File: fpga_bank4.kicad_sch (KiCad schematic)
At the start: 2 parts, among them U2 XC7A50T-FGG484

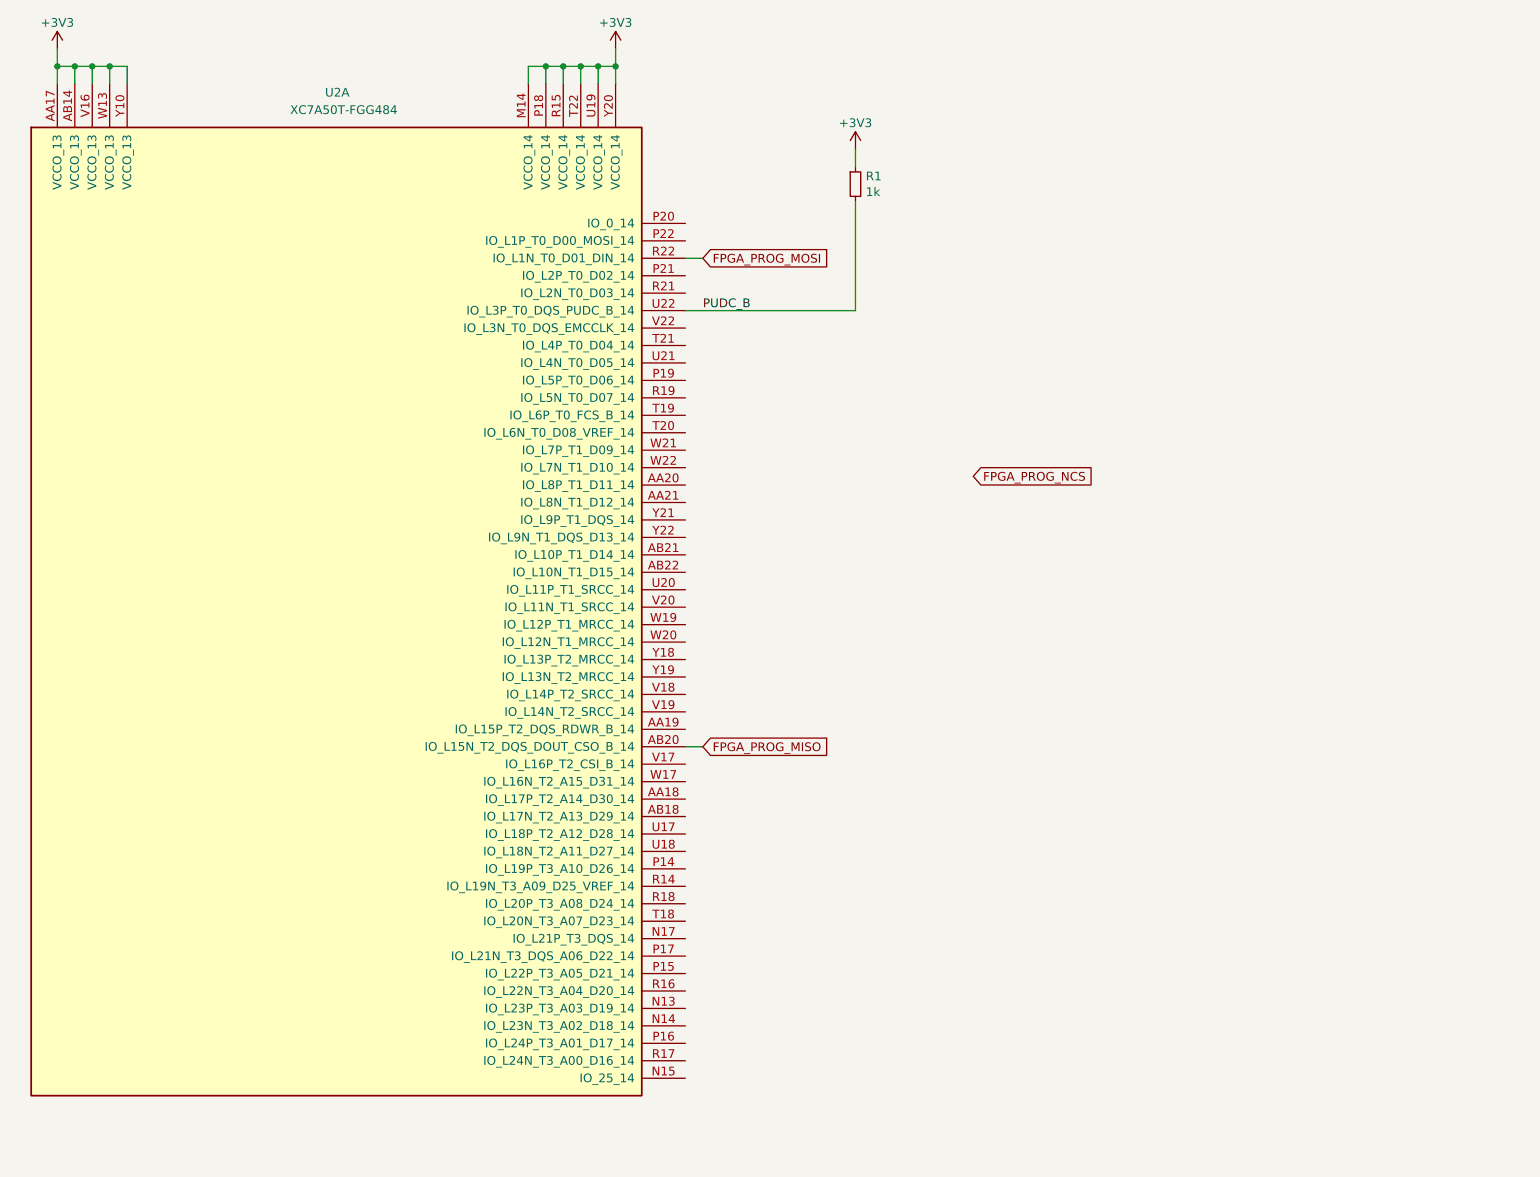
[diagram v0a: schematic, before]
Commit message: Changed FPGA to new package and hooked up some more pins
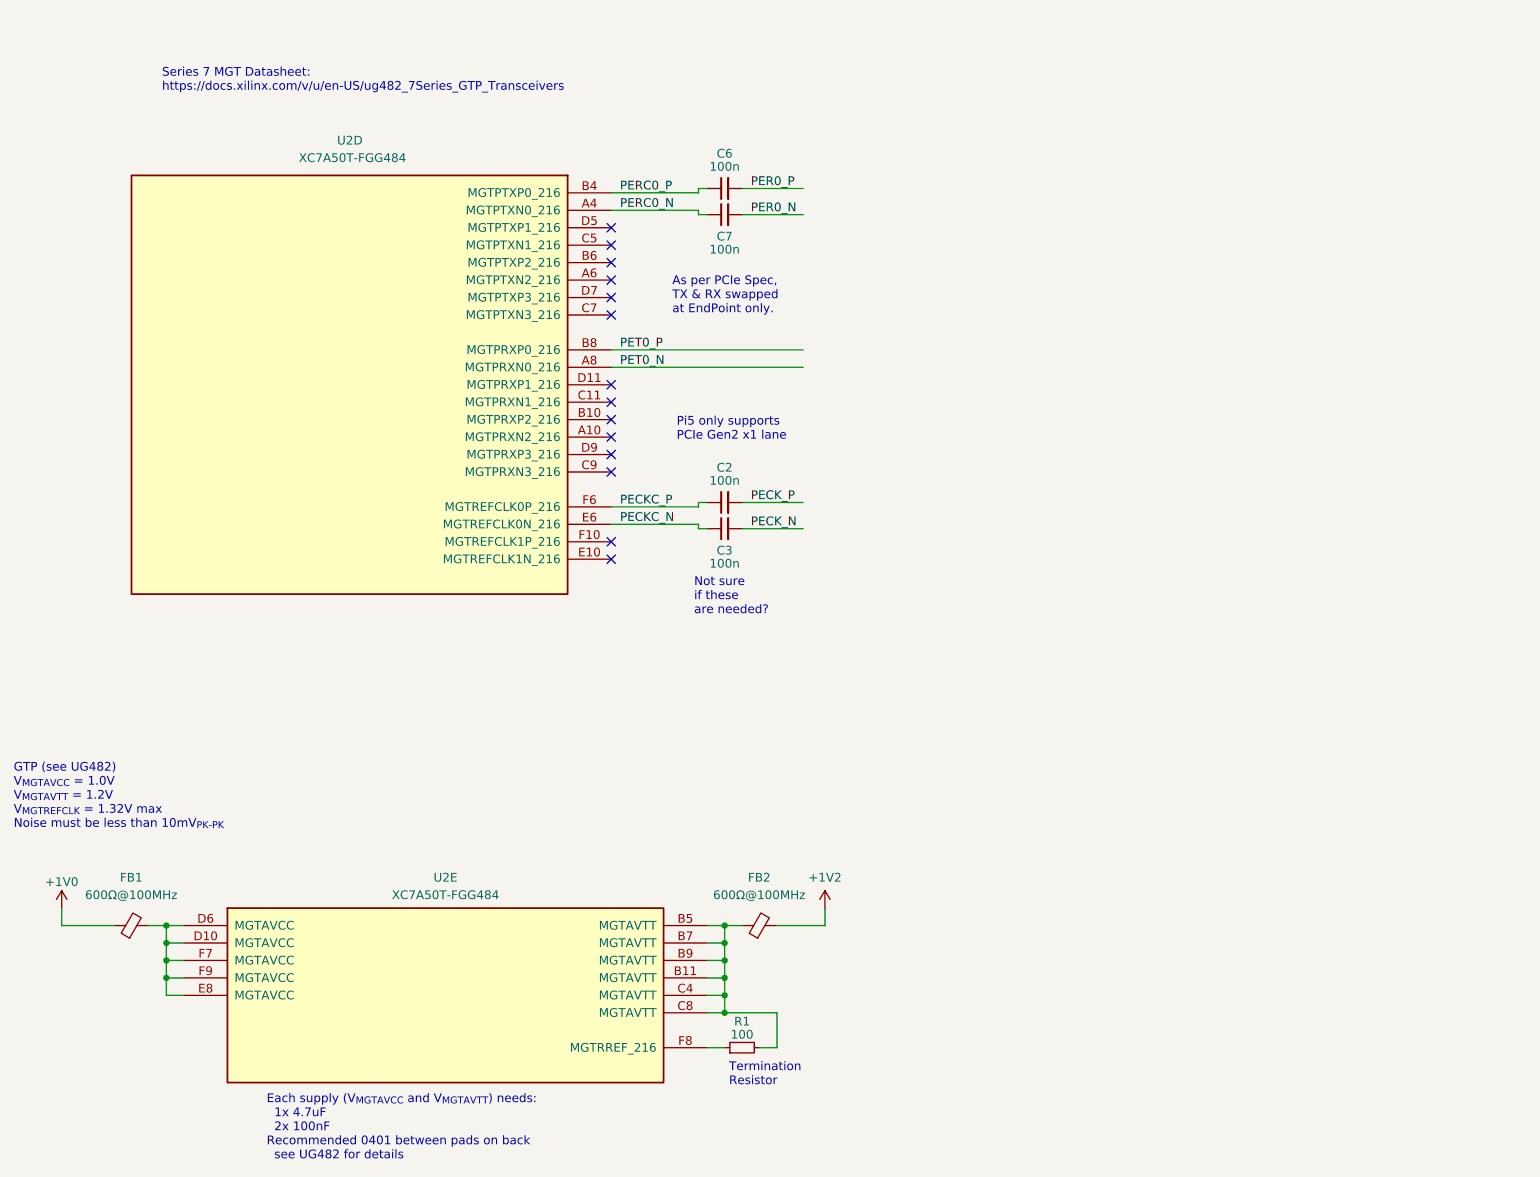
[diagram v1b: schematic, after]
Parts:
- removed U2: XC7A50T-FGG484, Package_BGA:Xilinx_FGG484, symbol FPGA_Xilinx_Artix7:XC7A50T-FGG484
- added C2, C3, C6, C7: 100n, Capacitor_SMD:C_0402_1005Metric_Pad0.74x0.62mm_HandSolder, symbol Device:C_Small
- added FB1, FB2: 600Ω@100MHz, Inductor_SMD:L_0603_1608Metric_Pad1.05x0.95mm_HandSolder, symbol Device:FerriteBead_Small
- added U2: XC7A50T-FGG484, Package_BGA:Xilinx_FGG484, symbol FPGA_Xilinx_Artix7:XC7A50T-FGG484
- R1: value 1k -> 100; LCSC C21190 -> C22775
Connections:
- net +3V3: no longer names the net of R1.1
- net +3V3: now also U2.F8 (MGTRREF_216)
- net PUDC_B: no longer names the net of R1.2
- net PUDC_B: now also FB2.1, U2.B11 (MGTAVTT), U2.B5 (MGTAVTT), U2.B7 (MGTAVTT), U2.B9 (MGTAVTT), U2.C4 (MGTAVTT), U2.C8 (MGTAVTT)
- new net: FB1.2, U2.D10 (MGTAVCC), U2.D6 (MGTAVCC), U2.E8 (MGTAVCC), U2.F7 (MGTAVCC), U2.F9 (MGTAVCC)
- new net +1V0: FB1.1
- new net +1V2: FB2.2
- new net PECKC_N: C3.1, U2.E6 (MGTREFCLK0N_216)
- new net PECKC_P: C2.1, U2.F6 (MGTREFCLK0P_216)
- new net PECK_N: C3.2
- new net PECK_P: C2.2
- new net PER0_N: C7.2
- new net PER0_P: C6.2
- new net PERC0_N: C7.1, U2.A4 (MGTPTXN0_216)
- new net PERC0_P: C6.1, U2.B4 (MGTPTXP0_216)
- new net PET0_N: U2.A8 (MGTPRXN0_216)
- new net PET0_P: U2.B8 (MGTPRXP0_216)
- no-connect marks 0 -> 14
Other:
- note added: "As per PCIe Spec, TX & RX swapped at EndPoint only."
- note added: "Each supply (V_{MGTAVCC} and V_{MGTAVTT}) needs: 1x 4.7uF 2x 100nF Recommended 0401 between pads on back see UG482 for details"
- note added: "GTP (see UG482) V_{MGTAVCC} = 1.0V V_{MGTAVTT} = 1.2V V_{MGTREFCLK} = 1.32V max Noise must be less than 10mV_{PK-PK}"
- note added: "Not sure if these are needed?"
- note added: "Pi5 only supports PCIe Gen2 x1 lane"
- note added: "Series 7 MGT Datasheet: https://docs.xilinx.com/v/u/en-US/ug482_7Series_GTP_Transceivers"
- note added: "Termination Resistor"
- title: FPGA Bank 14 -> FPGA Bank 216 (PCIe MGTs)

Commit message: Schematic finished, starting layout
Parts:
- added C10, C15: 4.7u, Capacitor_SMD:C_0402_1005Metric_Pad0.74x0.62mm_HandSolder, symbol Device:C_Small
- added C11, C12, C4, C5: 100n, Capacitor_SMD:C_0402_1005Metric_Pad0.74x0.62mm_HandSolder, symbol Device:C_Small
- R13: renamed from R1; footprint Resistor_SMD:R_0603_1608Metric_Pad0.98x0.95mm_HandSolder -> Resistor_SMD:R_0402_1005Metric_Pad0.72x0.64mm_HandSolder; LCSC C22775 -> (none)
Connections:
- net PERC0_N: now also U2.C7 (MGTPTXN3_216); no longer U2.A4 (MGTPTXN0_216)
- net PERC0_P: now also U2.D7 (MGTPTXP3_216); no longer U2.B4 (MGTPTXP0_216)
- net at FB2.1, R13.2, U2.B11 (MGTAVTT)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: now also C10.2, C4.2, C5.2
- net at FB1.2, U2.D10 (MGTAVCC), U2.D6 (MGTAVCC)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: now also C11.2, C12.2, C15.2
- net PCIE_TX0N: now reaches U2.C9 (MGTPRXN3_216)
- net PCIE_TX0P: now reaches U2.D9 (MGTPRXP3_216)
- net PECK_N renamed PCIE_CLKN
- net PECK_P renamed PCIE_CLKP
- net PER0_N renamed PCIE_RX0N
- net PER0_P renamed PCIE_RX0P
- net PET0_N: no longer names the net of U2.A8 (MGTPRXN0_216)
- net PET0_P: no longer names the net of U2.B8 (MGTPRXP0_216)
- new net GND: C10.1, C11.1, C12.1, C15.1, C4.1, C5.1
- no-connect marks 14 -> 15
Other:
- note added: "--->>"
- note added: "<<---"
- note added: "MGTAVCC - 0.1 uF Cap1: D6-C6 Cap2: D10-C10"
- note added: "MGTAVTT - 0.1 uF Cap3: C4-C3 Cap4: B11-B12"
- note added: "Pi5 only x1 lane"
- note added: "Series 7 MGT Datasheets: https://docs.xilinx.com/v/u/en-US/ug482_7Series_GTP_Transceivers pg054-7series-pcie-en-us-3.3"
- note added: "Test build: | C7 | pci_exp_txn[0] | MGTPTXN3_216 | C9 | pci_exp_rxn[0] | MGTPRXN3_216 | D7 | pci_exp_txp[0] | MGTPTXP3_216 | D9 | pci_exp_rxp[0] | MGTPRXP3_216 | E6 | sys_clk_n | MGTREFCLK0N_216 | F6 | sys_clk_p | MGTREFCLK0P_216"
- note removed: "GTP (see UG482) V_{MGTAVCC} = 1.0V V_{MGTAVTT} = 1.2V V_{MGTREFCLK} = 1.32V max Noise must be less than 10mV_{PK-PK}"
- note removed: "Not sure if these are needed?"
- note removed: "Pi5 only supports PCIe Gen2 x1 lane"
- note removed: "Series 7 MGT Datasheet: https://docs.xilinx.com/v/u/en-US/ug482_7Series_GTP_Transceivers"
- title: FPGA Bank 216 (PCIe MGTs) -> FPGA Power
- moved on the sheet: C2, C3, FB1, FB2, R13, U2D, U2E

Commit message: Updated titleblock texts
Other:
- title: FPGA Power -> FPGA Bank 216 (MGT/PCIe)
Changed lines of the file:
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@@
   (paper "A4")
   (title_block
-    (title "FPGA Power")
-    (date "2024-02-11")
+    (title "FPGA Bank 216 (MGT/PCIe)")
+    (date "2024-02-14")
     (rev "0.1")
     (company "George Smart, M1GEO")

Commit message: Started routing. More to go
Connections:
- net MGTAVTT: now reaches C10.2, C4.2, C5.2, FB2.1, R13.2, U2.B11 (MGTAVTT), U2.B5 (MGTAVTT), U2.B7 (MGTAVTT), U2.B9 (MGTAVTT), U2.C4 (MGTAVTT), U2.C8 (MGTAVTT)
- net MGTAVCC: now reaches C11.2, C12.2, C15.2, FB1.2, U2.D10 (MGTAVCC), U2.D6 (MGTAVCC), U2.E8 (MGTAVCC), U2.F7 (MGTAVCC), U2.F9 (MGTAVCC)
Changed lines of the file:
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@@
     )
   )
-  (text "MGTAVTT - 0.1 uF\nCap3: C4-C3\nCap4: B11-B12" (at 195.58 129.54 0)
+  (text "MGTAVTT - 0.1 uF\nCap3: C4-C3\nCap4: B11-B12" (at 193.675 127.635 0)
     (effects (font (size 1.27 1.27)) (justify left bottom))
   )
@@
     (effects (font (size 1.27 1.27)) (justify left bottom))
   )
-  (text "Pi5 only\nx1 lane\n" (at 129.54 72.39 0)
+  (text "Pi5 only\nx1 lane\n" (at 133.35 74.295 0)
     (effects (font (size 1.27 1.27)) (justify left bottom))
   )
@@
     (effects (font (size 2 2)) (justify right bottom))
   )
-  (text "MGTAVCC - 0.1 uF\nCap1: D6-C6\nCap2: D10-C10" (at 93.98 129.54 0)
+  (text "MGTAVCC - 0.1 uF\nCap1: D6-C6\nCap2: D10-C10" (at 95.25 127.635 0)
     (effects (font (size 1.27 1.27)) (justify left bottom))
   )
   (text "As per PCIe Spec,\nTX & RX swapped\nat EndPoint only."
-    (at 126.365 53.975 0)
+    (at 107.95 75.565 0)
     (effects (font (size 1.27 1.27)) (justify left bottom))
   )
@@
     (effects (font (size 1.27 1.27)) (justify left bottom))
   )
+  (label "MGTAVCC" (at 97.79 130.81 0) (fields_autoplaced)
+    (effects (font (size 1.27 1.27)) (justify left bottom))
+  )
   (label "PECKC_N" (at 100.965 90.17 0) (fields_autoplaced)
     (effects (font (size 1.27 1.27)) (justify left bottom))
@@
     (effects (font (size 1.27 1.27)) (justify left bottom))
   )
+  (label "MGTAVTT" (at 196.85 130.81 0) (fields_autoplaced)
+    (effects (font (size 1.27 1.27)) (justify left bottom))
+  )

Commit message: More routing and tinkering. Need to do non-MGT decoupling next.
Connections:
- net MR: now reaches R13.1, U2.F8 (MGTRREF_216)
- net +1V0 renamed +1V0_MGTAVCC
- net +1V2 renamed +1V2_MGTAVTT
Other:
- moved on the sheet: R13
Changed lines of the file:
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@@
-    (stroke (width 0) (type default))
-  )
-  (wire (pts (xy 196.85 148.59) (xy 199.39 148.59))
     (stroke (width 0) (type default))
   )
@@
     (stroke (width 0) (type default))
   )
-  (wire (pts (xy 199.39 148.59) (xy 199.39 143.51))
+  (wire (pts (xy 200.66 148.59) (xy 200.66 143.51))
     (stroke (width 0) (type default))
   )
@@
     (stroke (width 0) (type default))
   )
-  (wire (pts (xy 189.23 148.59) (xy 191.77 148.59))
+  (wire (pts (xy 189.23 148.59) (xy 194.31 148.59))
+    (stroke (width 0) (type default))
+  )
+  (wire (pts (xy 200.66 148.59) (xy 199.39 148.59))
     (stroke (width 0) (type default))
   )
@@
     (stroke (width 0) (type default))
   )
-  (wire (pts (xy 199.39 143.51) (xy 191.77 143.51))
+  (wire (pts (xy 200.66 143.51) (xy 191.77 143.51))
     (stroke (width 0) (type default))
   )
@@
     (effects (font (size 1.27 1.27)) (justify left bottom))
   )
+  (label "MR" (at 190.5 148.59 0) (fields_autoplaced)
+    (effects (font (size 1.27 1.27)) (justify left bottom))
+  )
   (label "MGTAVTT" (at 196.85 130.81 0) (fields_autoplaced)
     (effects (font (size 1.27 1.27)) (justify left bottom))
@@
     )
   )
-  (symbol (lib_name "+1V2_1") (lib_id "power:+1V2") (at 232.41 125.73 0) (unit 1)
-    (in_bom yes) (on_board yes) (dnp no) (fields_autoplaced)
-    (property "Reference" "#PWR037" (at 232.41 129.54 0)
-      (effects (font (size 1.27 1.27)) hide)
-    )
-    (property "Value" "+1V2_MGTAVTT" (at 232.41 121.285 0)
-      (effects (font (size 1.27 1.27)))
-    )
-    (property "Footprint" "" (at 232.41 125.73 0)
-      (effects (font (size 1.27 1.27)) hide)
-    )
-    (property "Datasheet" "" (at 232.41 125.73 0)
-      (effects (font (size 1.27 1.27)) hide)
-    )
-    (pin "1")
-    (instances
-      (project "Pi5-Artix50T-Hat"
-        (path "/e63e39d7-6ac0-4ffd-8aa3-1841a4541b55/58f29d61-b732-4149-afb6-3ea37966fd1b/9687875a-5c78-4c5f-9fe3-711f7f6d52bf"
-          (reference "#PWR037") (unit 1)
-        )
-      )
-    )
-  )
   (symbol (lib_id "Device:C_Small") (at 116.205 56.515 90) (unit 1)
     (in_bom yes) (on_board yes) (dnp no)
@@
     )
   )
-  (symbol (lib_id "Device:R_Small") (at 194.31 148.59 90) (unit 1)
+  (symbol (lib_id "fpga_mgt_power:+1V0_MGTAVCC") (at 71.12 125.73 0) (unit 1)
     (in_bom yes) (on_board yes) (dnp no)
-    (property "Reference" "R13" (at 194.31 144.78 90)
+    (property "Reference" "#PWR048" (at 71.12 129.54 0)
+      (effects (font (size 1.27 1.27)) hide)
+    )
+    (property "Value" "+1V0_MGTAVCC" (at 71.12 121.92 0)
       (effects (font (size 1.27 1.27)))
     )
-    (property "Value" "100" (at 194.31 146.685 90)
+    (property "Footprint" "" (at 71.12 125.73 0)
+      (effects (font (size 1.27 1.27)) hide)
+    )
+    (property "Datasheet" "" (at 71.12 125.73 0)
+      (effects (font (size 1.27 1.27)) hide)
+    )
+    (pin "1")
+    (instances
+      (project "Pi5-Artix50T-Hat"
+        (path "/e63e39d7-6ac0-4ffd-8aa3-1841a4541b55/58f29d61-b732-4149-afb6-3ea37966fd1b/9687875a-5c78-4c5f-9fe3-711f7f6d52bf"
+          (reference "#PWR048") (unit 1)
+        )
+      )
+    )
+  )
+  (symbol (lib_id "fpga_mgt_power:+1V2_MGTAVTT") (at 232.41 125.73 0) (unit 1)
+    (in_bom yes) (on_board yes) (dnp no)
+    (property "Reference" "#PWR049" (at 232.41 129.54 0)
+      (effects (font (size 1.27 1.27)) hide)
+    )
+    (property "Value" "+1V2_MGTAVTT" (at 232.41 121.92 0)
       (effects (font (size 1.27 1.27)))
     )
-    (property "Footprint" "Resistor_SMD:R_0402_1005Metric_Pad0.72x0.64mm_HandSolder" (at 194.31 148.59 0)
-      (effects (font (size 1.27 1.27)) hide)
-    )
-    (property "Datasheet" "" (at 194.31 148.59 0)
-      (effects (font (size 1.27 1.27)) hide)
-    )
-    (property "LCSC" "" (at 194.31 148.59 0)
+    (property "Footprint" "" (at 232.41 125.73 0)
+      (effects (font (size 1.27 1.27)) hide)
+    )
+    (property "Datasheet" "" (at 232.41 125.73 0)
+      (effects (font (size 1.27 1.27)) hide)
+    )
+    (pin "1")
+    (instances
+      (project "Pi5-Artix50T-Hat"
+        (path "/e63e39d7-6ac0-4ffd-8aa3-1841a4541b55/58f29d61-b732-4149-afb6-3ea37966fd1b/9687875a-5c78-4c5f-9fe3-711f7f6d52bf"
+          (reference "#PWR049") (unit 1)
+        )
+      )
+    )
+  )
+  (symbol (lib_id "Device:R_Small") (at 196.85 148.59 90) (unit 1)
+    (in_bom yes) (on_board yes) (dnp no)
+    (property "Reference" "R13" (at 196.85 144.78 90)
+      (effects (font (size 1.27 1.27)))
+    )
+    (property "Value" "100" (at 196.85 146.685 90)
+      (effects (font (size 1.27 1.27)))
+    )
+    (property "Footprint" "Resistor_SMD:R_0402_1005Metric_Pad0.72x0.64mm_HandSolder" (at 196.85 148.59 0)
+      (effects (font (size 1.27 1.27)) hide)
+    )
+    (property "Datasheet" "" (at 196.85 148.59 0)
+      (effects (font (size 1.27 1.27)) hide)
+    )
+    (property "LCSC" "" (at 196.85 148.59 0)
       (effects (font (size 1.27 1.27)) hide)
     )
@@
         )
       )
-    )
-  )
-  (symbol (lib_name "+1V0_1") (lib_id "power:+1V0") (at 71.12 125.73 0) (unit 1)
-    (in_bom yes) (on_board yes) (dnp no)
-    (property "Reference" "#PWR030" (at 71.12 129.54 0)
-      (effects (font (size 1.27 1.27)) hide)
-    )
-    (property "Value" "+1V0_MGTAVCC" (at 71.12 121.92 0)
-      (effects (font (size 1.27 1.27)))
-    )
-    (property "Footprint" "" (at 71.12 125.73 0)
-      (effects (font (size 1.27 1.27)) hide)
-    )
-    (property "Datasheet" "" (at 71.12 125.73 0)
-      (effects (font (size 1.27 1.27)) hide)
-    )
-    (pin "1")
-    (instances
-      (project "Pi5-Artix50T-Hat"
-        (path "/e63e39d7-6ac0-4ffd-8aa3-1841a4541b55/58f29d61-b732-4149-afb6-3ea37966fd1b/9687875a-5c78-4c5f-9fe3-711f7f6d52bf"
-          (reference "#PWR030") (unit 1)
-        )
-      )
